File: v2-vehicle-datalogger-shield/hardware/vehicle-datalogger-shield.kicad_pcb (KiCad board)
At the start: 2 copper layers, 68.6 x 53.3 mm, 14 parts, among them J1 CONN-SD-CARD-PUSH-PULL-R/A-SMD, J2 FONA808-GPS, J3 OBDII-UART, U1 HOLE, U2 HOLE, U3 HOLE, U4 HOLE, U5 ARDUINO-101-SHIELD

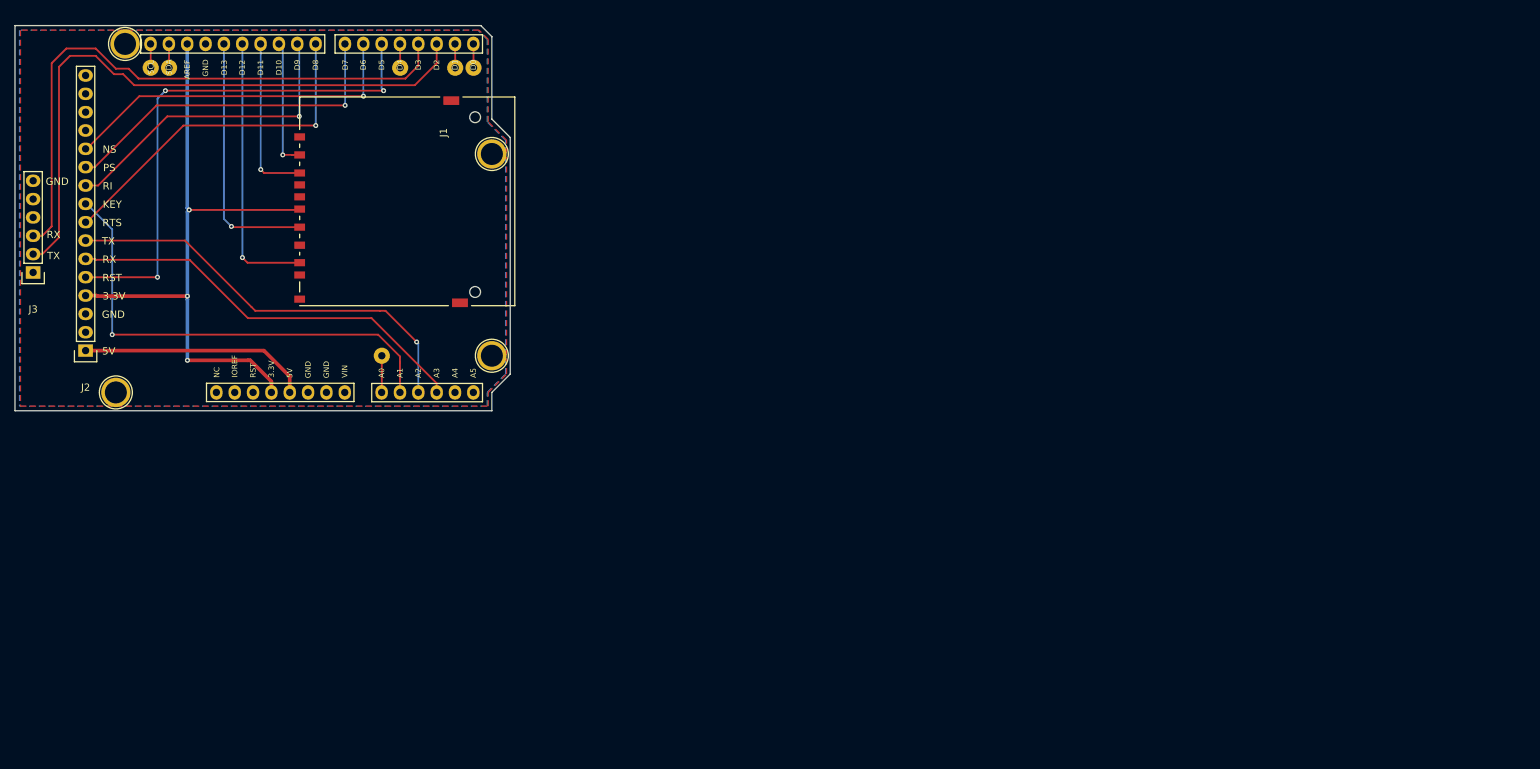
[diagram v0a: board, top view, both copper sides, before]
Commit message: Updated schematic, BOM, and spread out footprints. Ready to layout.
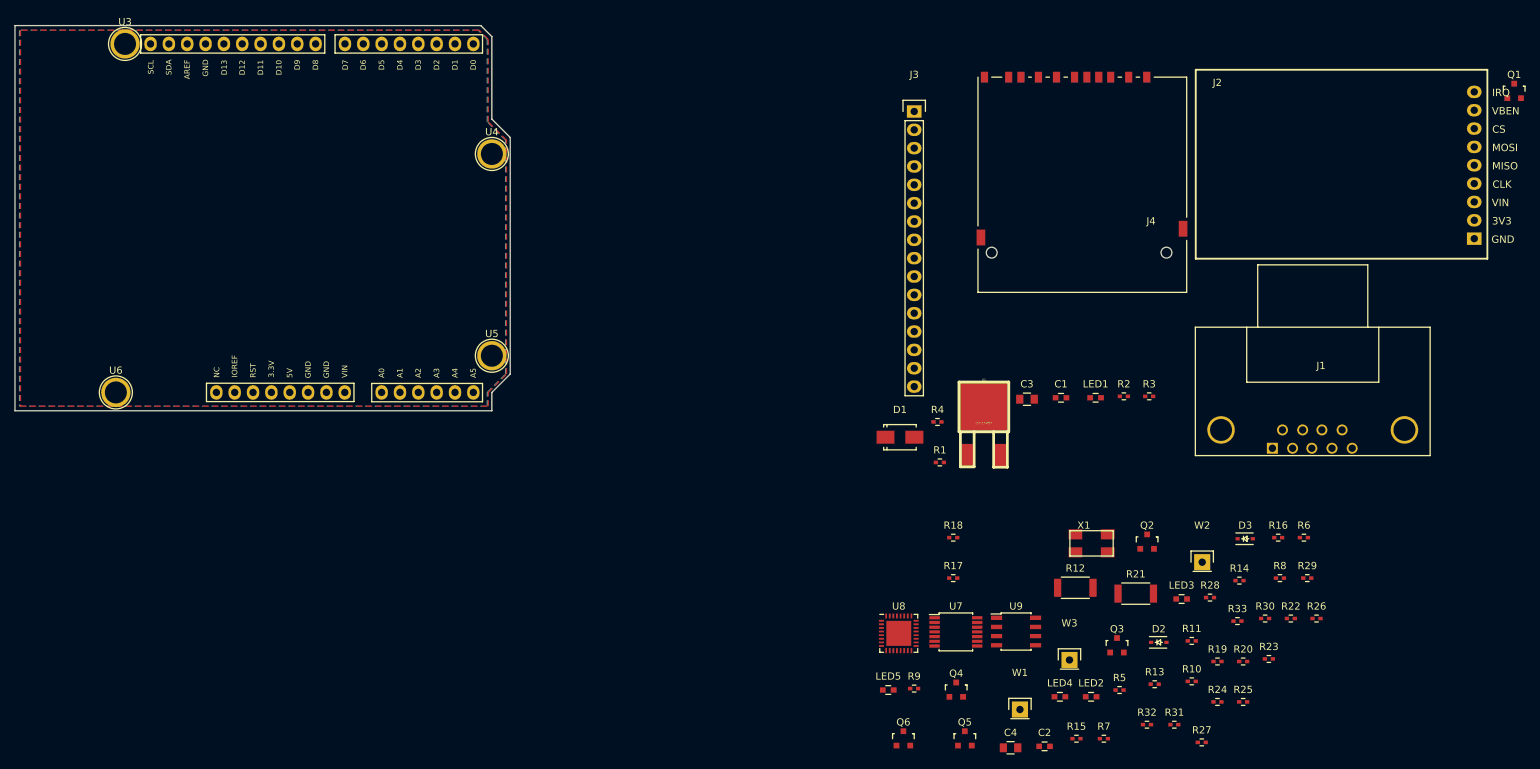
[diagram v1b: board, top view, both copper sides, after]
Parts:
- removed the U5 at (133.8, 123.8)
- removed W4: A4, Wickerlib:TestHole_1x01
- removed W5: D4, Wickerlib:TestHole_1x01
- removed W6: A5, Wickerlib:TestHole_1x01
- added C1: 100nF, Wickerlib:0603, F.Cu at (255.8, 124.6)
- added C2: 100nF, Wickerlib:0603, F.Cu at (253.6, 172.8)
- added C3: 1uF, Wickerlib:0805, F.Cu at (251.1, 124.8)
- added C4: 1uF, Wickerlib:0805, F.Cu at (248.9, 173.0)
- added D1: MBRA140, Wickerlib:Diode_SMA, F.Cu at (233.5, 130.0)
- added D2: BAS16, Wickerlib:SOD-323, F.Cu at (269.4, 158.4)
- added D3: BAS16, Wickerlib:SOD-323, F.Cu at (281.4, 144.1)
- added J4: CONN-SD-CARD-PUSH-PULL-R/A-SMD, Wickerlib:SD_Holder_FullSize, F.Cu at (258.4, 80.2)
- added LED1: RED, Wickerlib:0603, F.Cu at (260.6, 124.6)
- added LED2: RED, Wickerlib:0603, F.Cu at (260.0, 166.0)
- added LED3: YEL, Wickerlib:0603, F.Cu at (272.6, 152.4)
- added LED4: RED, Wickerlib:0603, F.Cu at (255.7, 166.0)
- added LED5: YEL, Wickerlib:0603, F.Cu at (231.9, 165.0)
- added Q1: BSS138, Wickerlib:SOT-23-3, F.Cu at (318.6, 82.1)
- added Q2: MMBT2222, Wickerlib:SOT-23-3, F.Cu at (267.8, 144.5)
- added Q3: BSS138, Wickerlib:SOT-23-3, F.Cu at (263.6, 158.8)
- added Q4: IRLML2246, Wickerlib:SOT-23-3, F.Cu at (241.3, 165.0)
- added Q5: MMBT2222, Wickerlib:SOT-23-3, F.Cu at (242.5, 171.7)
- added Q6: MMBT2222, Wickerlib:SOT-23-3, F.Cu at (234.0, 171.7)
- added R1: 866, Wickerlib:0402, F.Cu at (239.1, 133.5)
- added R10: 10K, Wickerlib:0402, F.Cu at (274.0, 163.8)
- added R11: 10K, Wickerlib:0402, F.Cu at (274.0, 158.2)
- added R12: 510 1/2W, Wickerlib:2010, F.Cu at (257.8, 150.9)
- added R13: 1.5K, Wickerlib:0402, F.Cu at (268.8, 164.2)
- added R14: 10K, Wickerlib:0402, F.Cu at (280.6, 149.9)
- added R15: 10K, Wickerlib:0402, F.Cu at (258.0, 171.8)
- added R16: 10K, Wickerlib:0402, F.Cu at (285.9, 143.9)
- added R17: RES-10K-1%-1/10W-0402, Wickerlib:0402, F.Cu at (240.9, 149.5)
- added R18: RES-10K-1%-1/10W-0402, Wickerlib:0402, F.Cu at (240.9, 143.9)
- added R19: 10K, Wickerlib:0402, F.Cu at (277.5, 161.1)
- added R2: 374, Wickerlib:0402, F.Cu at (264.6, 124.4)
- added R20: 1K, Wickerlib:0402, F.Cu at (281.1, 161.1)
- added R21: 510 1/2W, Wickerlib:2010, F.Cu at (266.2, 151.7)
- added R22: 1K, Wickerlib:0402, F.Cu at (287.7, 155.1)
- added R23: 10K, Wickerlib:0402, F.Cu at (284.6, 160.7)
- added R24: 10K, Wickerlib:0402, F.Cu at (277.5, 166.7)
- added R25: 62K, Wickerlib:0402, F.Cu at (281.1, 166.7)
- added R26: 10K, Wickerlib:0402, F.Cu at (291.2, 155.1)
- added R27: 4.7K, Wickerlib:0402, F.Cu at (275.3, 172.3)
- added R28: 330, Wickerlib:0402, F.Cu at (276.5, 152.2)
- added R29: 330, Wickerlib:0402, F.Cu at (290.0, 149.5)
- added R3: 240, Wickerlib:0402, F.Cu at (268.1, 124.4)
- added R30: 330, Wickerlib:0402, F.Cu at (284.1, 155.1)
- added R31: 330, Wickerlib:0402, F.Cu at (271.5, 169.8)
- added R32: 4.7K, Wickerlib:0402, F.Cu at (267.8, 169.8)
- added R33: 1.5K, Wickerlib:0402, F.Cu at (280.3, 155.5)
- added R4: 1K, Wickerlib:0402, F.Cu at (238.7, 127.9)
- added R5: 10K, Wickerlib:0402, F.Cu at (264.0, 165.0)
- added R6: 10K, Wickerlib:0402, F.Cu at (289.5, 143.9)
- added R7: 1.2K, Wickerlib:0402, F.Cu at (261.8, 171.8)
- added R8: 4.7K, Wickerlib:0402, F.Cu at (286.2, 149.5)
- added R9: 1K, Wickerlib:0402, F.Cu at (235.5, 164.8)
- added U1: LM317MDT, Wickerlib:DPAK, F.Cu at (245.2, 132.5)
- added U2: ARDUINO-101-SHIELD, Wickerlib:ARDUINO-101-SHIELD, F.Cu at (133.8, 123.8)
- added U7: LM339PWR, Wickerlib:TSSOP-14_4.4x5mm_Pitch0.65mm, F.Cu at (241.3, 157.0)
- added U8: STN1110, Wickerlib:QFN-32-1EP_5x5mm_Pitch0.5mm, F.Cu at (233.4, 157.2)
- added U9: MCP2551, Wickerlib:SOIC-8_3.9x4.9mm_Pitch1.27mm, F.Cu at (249.6, 156.9)
- added X1: 16MHz 18pF, Wickerlib:CRYSTAL-CTS-4SMD, F.Cu at (257.1, 146.5)
- J1: value CONN-SD-CARD-PUSH-PULL-R/A-SMD -> DB9 TO ENGINE CONTROL UNIT; footprint Wickerlib:SD_Holder_FullSize -> Wickerlib:DB9FC
- J2: value FONA808-GPS -> CC3000-HUZZAH; footprint Wickerlib:Pin_Header_Straight_1x16 -> Wickerlib:CC3000BKOUT
- J3: value OBDII-UART -> FONA808-GPS; footprint Wickerlib:Pin_Header_Straight_1x06 -> Wickerlib:Pin_Header_Straight_1x16
- W1: value D0 -> TEST_1P; footprint Wickerlib:TestHole_1x01 -> Wickerlib:Pin_Header_Straight_1x01
- W2: value A0 -> TEST_1P; footprint Wickerlib:TestHole_1x01 -> Wickerlib:Pin_Header_Straight_1x01
- W3: value D1 -> TEST_1P; footprint Wickerlib:TestHole_1x01 -> Wickerlib:Pin_Header_Straight_1x01
- moved J2 198.0 mm to (314.9, 79.1), turned to 0 degrees
- moved J1 143.9 mm to (290.6, 130.3), turned to 0 degrees
- moved J3 124.0 mm to (235.5, 84.9), turned to 0 degrees
- moved W3 118.2 mm to (257.0, 160.9)
- moved W2 117.1 mm to (275.4, 147.3)
- moved W1 116.7 mm to (250.2, 167.7)
- renumbered U2 to U5, U1 to U6
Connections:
- J1 pad 1: /D10(SD_CS) -> GND
- J1 pad 2: /D11(MOSI) -> GND
- J1 pad 3: GND -> CAN_HI
- J1 pad 4: +3V3 -> K_LINE
- J1 pad 5: /D13(SCLK) -> CAN_LO
- J1 pad 6: GND -> J1850BUS-
- J1 pad 7: /D12(MISO) -> J1850BUS+
- J1 pad 8: (no net) -> L_LINE
- J1 pad 9: (no net) -> Net-(D1-Pad2)
- J2 pad 1: +5V -> GND
- J2 pad 2: (no net) -> +3V3
- J2 pad 3: GND -> (no net)
- J2 pad 4: +3V3 -> /D13(SCLK)
- J2 pad 5: /D5(FONA_RST) -> /D12(MISO)
- J2 pad 6: /A3(FONA_RX) -> /D11(MOSI)
- J2 pad 7: /A2(FONA_TX) -> /A4(WIFI_CS)
- J2 pad 8: /D8(FONA_RTS) -> /D4(WIFI_VBEN)
- J2 pad 9: /A1(FONA_KEY) -> /A0(WIFI_IRQ)
- J3 pad 1: (no net) -> +5V
- J3 pad 2: /D2(OBD2_TX) -> (no net)
- J3 pad 3: /D3(OBD2_RX) -> GND
- J3 pad 4: (no net) -> +3V3
- J3 pad 5: (no net) -> /D5(FONA_RST)
- J3 pad 6: GND -> /A3(FONA_RX)
- W1 pad 1: /D0 -> /Vehicle Datalogger/RESET
- W2 pad 1: /A0 -> /Vehicle Datalogger/SLEEP
- W3 pad 1: /D1 -> /Vehicle Datalogger/~PWR_CTRL
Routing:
- net +3V3: track 88.0 -> 0.00 mm, vias 3 -> 0
- net /D2(OBD2_TX): track 86.7 -> 0.00 mm
- net /D3(OBD2_RX): track 82.8 -> 0.00 mm
- net /D5(FONA_RST): track 73.1 -> 0.00 mm, vias 3 -> 0
- net /A1(FONA_KEY): track 66.0 -> 0.00 mm, vias 1 -> 0
- net /A2(FONA_TX): track 58.7 -> 0.00 mm, vias 1 -> 0
- net /A3(FONA_RX): track 57.0 -> 0.00 mm
- net /D6(FONA_NS): track 48.8 -> 0.00 mm, vias 1 -> 0
- net /D8(FONA_RTS): track 48.7 -> 0.00 mm, vias 1 -> 0
- net /D7(FONA_PS): track 48.0 -> 0.00 mm, vias 1 -> 0
- net /D9(FONA_RI): track 43.7 -> 0.00 mm, vias 1 -> 0
- net /D12(MISO): track 37.8 -> 0.00 mm, vias 1 -> 0
- net /D13(SCLK): track 35.2 -> 0.00 mm, vias 1 -> 0
- net +5V: track 32.0 -> 0.00 mm
- net /D11(MOSI): track 23.0 -> 0.00 mm, vias 1 -> 0
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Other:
- board text removed: "3.3V"
- board text removed: "5V"
- board text removed: "Arduino 101 Vehicle Logger Shield v1.0 J1: SD Card 2041021-4 J2: FONA808+GPS Breakout Board J3: OBDII-UART Adapter Board"
- board text removed: "GND"
- board text removed: "KEY"
- board text removed: "NS"
- board text removed: "PS"
- board text removed: "RI"
- board text removed: "RST"
- board text removed: "RTS"
- board text removed: "RX"
- board text removed: "TX"
- board text removed: "Wickerbox Electronics 2016"
